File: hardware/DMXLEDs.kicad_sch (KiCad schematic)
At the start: 16 parts

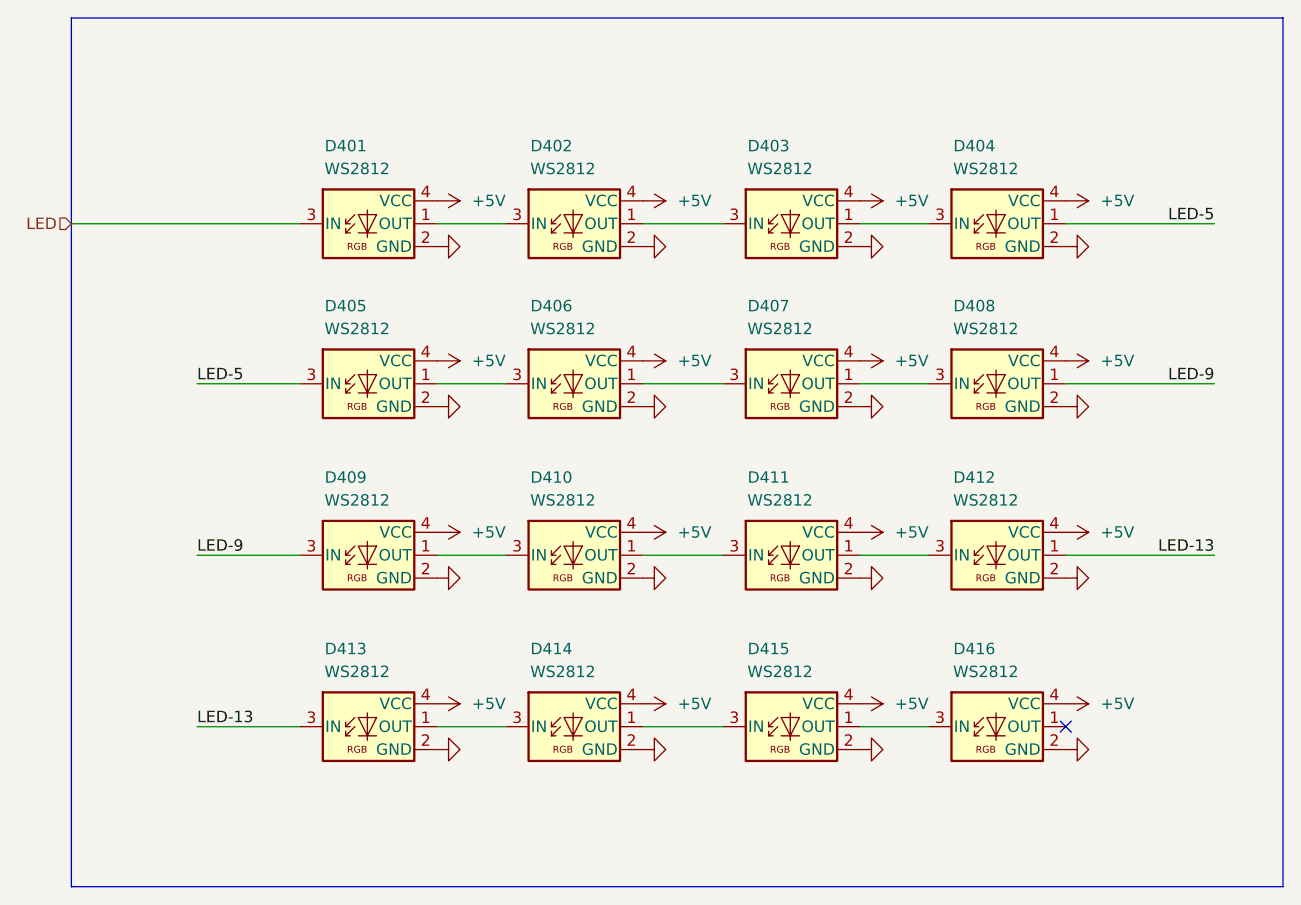
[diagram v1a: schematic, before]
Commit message: Update power symbols
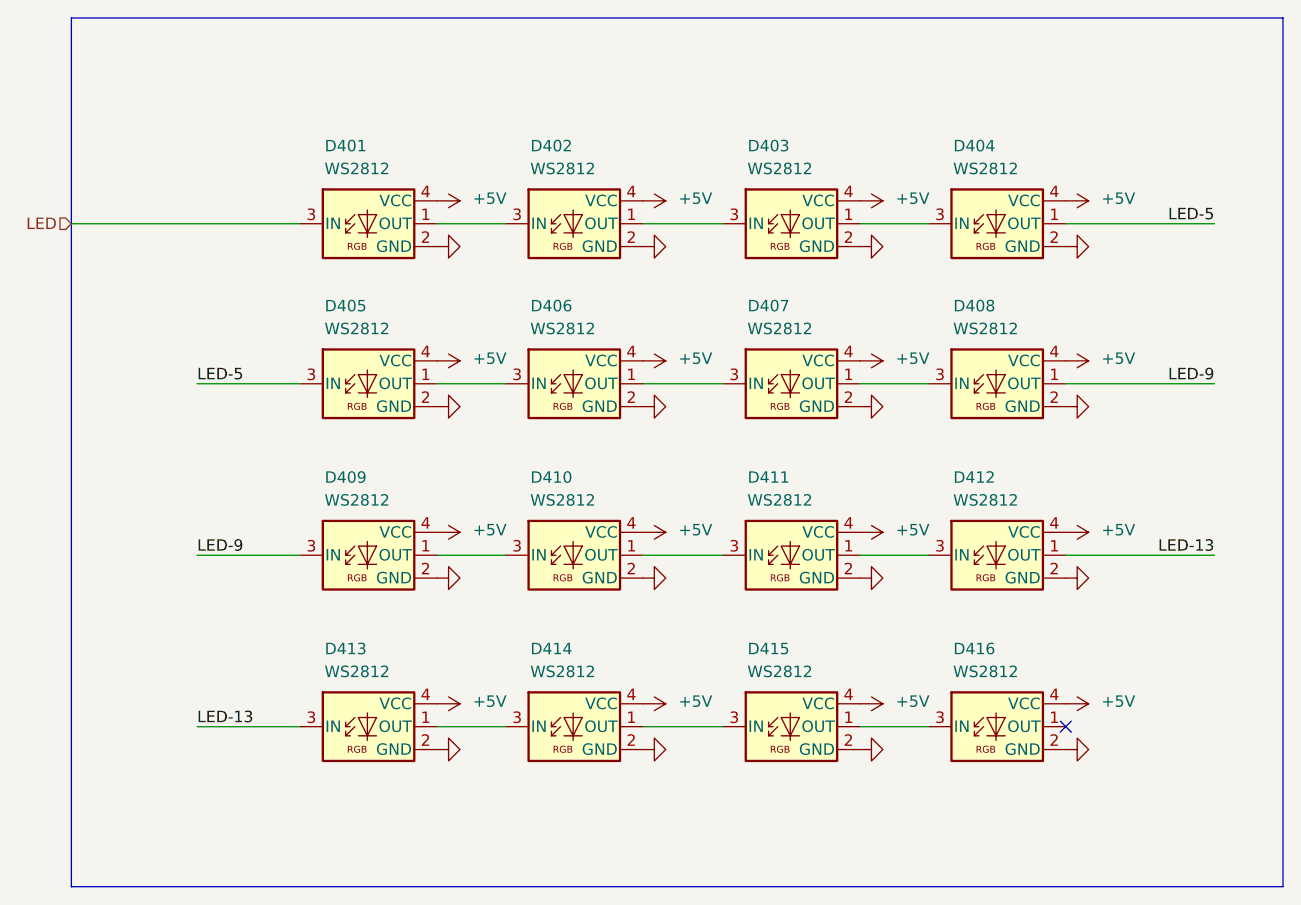
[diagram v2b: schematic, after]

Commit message: Update parts
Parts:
- D401, D402, D403, D404, D405, D406, D407, D408, D409, D410, D411, D412, D413, D414, D415, D416: LCSC (none) -> C965555; Manufacturer (none) -> Worldsemi; Product (none) -> WS2812B-2020

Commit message: Replace diode
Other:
- title: DMX LED -> V2 dmx

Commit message: Update
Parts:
- D401, D402, D403, D404, D405, D406, D407, D408, D409, D410, D411, D412, D413, D414, D415, D416: Id (none) -> LED:${SYMBOL_NAME}; Rating (none) -> 15mA
